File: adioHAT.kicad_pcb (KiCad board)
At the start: 2 copper layers, 65 x 56 mm, 29 parts, among them J1 Conn_01x01, J2 Conn_02x02_Odd_Even, J3 Conn_02x20_Odd_Even, J4 Conn_02x20_Odd_Even, U1 AD8603, U2 DAC7571, U3 AD5593R, U4 LM7321, U5 PCA9575D, U6 TXU0104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

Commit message: fixed i2c connections for ad5593
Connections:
- U3 pad 15: /SCL -> /SDA
- U3 pad 16: /SDA -> /SCL
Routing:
- net /SDA: track 55.2 -> 56.6 mm, vias 0 -> 2
- net /SCL: track 59.9 -> 59.2 mm
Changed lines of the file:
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@@
       (net 1 "GND") (pinfunction "GND") (pintype "power_in"))
     (pad "15" smd roundrect (at -0.25 -1.4375 270) (size 0.25 0.875) (layers "F.Cu" "F.Paste" "F.Mask") (roundrect_rratio 0.25)
-      (net 32 "/SCL") (pinfunction "SDA") (pintype "bidirectional"))
+      (net 31 "/SDA") (pinfunction "SDA") (pintype "bidirectional"))
     (pad "16" smd roundrect (at -0.75 -1.4375 270) (size 0.25 0.875) (layers "F.Cu" "F.Paste" "F.Mask") (roundrect_rratio 0.25)
-      (net 31 "/SDA") (pinfunction "SCL") (pintype "input"))
+      (net 32 "/SCL") (pinfunction "SCL") (pintype "input"))
     (model "${KICAD6_3DMODEL_DIR}/Package_CSP.3dshapes/LFCSP-16-1EP_3x3mm_P0.5mm_EP1.3x1.3mm.wrl"
       (offset (xyz 0 0 0))
@@
   (via (at 105.537 50.8) (size 0.6) (drill 0.3) (layers "F.Cu" "B.Cu") (free) (net 1))
   (via (at 125.7556 52.0956) (size 0.6) (drill 0.3) (layers "F.Cu" "B.Cu") (free) (net 1))
-  (via (at 140.8178 66.8784) (size 0.6) (drill 0.3) (layers "F.Cu" "B.Cu") (free) (net 1))
+  (via (at 141.351 67.31) (size 0.6) (drill 0.3) (layers "F.Cu" "B.Cu") (free) (net 1))
   (via (at 160.8584 60.0966) (size 0.6) (drill 0.3) (layers "F.Cu" "B.Cu") (free) (net 1))
   (via (at 160.274 81.661) (size 0.6) (drill 0.3) (layers "F.Cu" "B.Cu") (net 1))
@@
   (segment (start 128.69 48.77) (end 127.244 50.216) (width 0.3) (layer "B.Cu") (net 30))
   (segment (start 118.9126 69.6426) (end 114.797 65.527) (width 0.2) (layer "F.Cu") (net 31))
-  (segment (start 139.2965 67.9675) (end 139.7828 67.4812) (width 0.2) (layer "F.Cu") (net 31))
-  (segment (start 139.7828 65.2338) (end 138.811 64.262) (width 0.2) (layer "F.Cu") (net 31))
   (segment (start 135.745786 64.262) (end 117.983 64.262) (width 0.2) (layer "F.Cu") (net 31))
   (segment (start 135.755386 64.2716) (end 135.745786 64.262) (width 0.2) (layer "F.Cu") (net 31))
@@
   (segment (start 116.186 54.046) (end 116.186 62.465) (width 0.2) (layer "F.Cu") (net 31))
   (segment (start 116.186 62.465) (end 116.967 63.246) (width 0.2) (layer "F.Cu") (net 31))
+  (segment (start 138.852178 64.262) (end 139.121839 64.531661) (width 0.2) (layer "F.Cu") (net 31))
   (segment (start 117.983 64.262) (end 116.967 63.246) (width 0.2) (layer "F.Cu") (net 31))
-  (segment (start 139.7828 67.4812) (end 139.7828 65.2338) (width 0.2) (layer "F.Cu") (net 31))
+  (segment (start 139.616186 68.4675) (end 138.9653 68.4675) (width 0.2) (layer "F.Cu") (net 31))
   (segment (start 115.145896 65.527) (end 114.797 65.527) (width 0.2) (layer "F.Cu") (net 31))
   (segment (start 117.221 63.5) (end 117.172896 63.5) (width 0.2) (layer "F.Cu") (net 31))
   (segment (start 138.811 64.262) (end 136.593415 64.262) (width 0.2) (layer "F.Cu") (net 31))
   (segment (start 136.583814 64.2716) (end 135.755386 64.2716) (width 0.2) (layer "F.Cu") (net 31))
-  (segment (start 138.9653 67.9675) (end 139.2965 67.9675) (width 0.2) (layer "F.Cu") (net 31))
   (segment (start 110.91 48.77) (end 116.186 54.046) (width 0.2) (layer "F.Cu") (net 31))
   (segment (start 116.967 63.246) (end 117.221 63.5) (width 0.2) (layer "F.Cu") (net 31))
+  (segment (start 138.811 64.262) (end 138.852178 64.262) (width 0.2) (layer "F.Cu") (net 31))
   (segment (start 117.172896 63.5) (end 115.145896 65.527) (width 0.2) (layer "F.Cu") (net 31))
   (segment (start 118.9126 71.4912) (end 118.9126 69.6426) (width 0.2) (layer "F.Cu") (net 31))
-  (segment (start 136.41813 63.8716) (end 136.42773 63.862) (width 0.2) (layer "F.Cu") (net 32))
-  (segment (start 139.3 63.862) (end 140.1828 64.7448) (width 0.2) (layer "F.Cu") (net 32))
-  (segment (start 136.42773 63.862) (end 139.3 63.862) (width 0.2) (layer "F.Cu") (net 32))
+  (segment (start 140.567023 67.516663) (end 139.616186 68.4675) (width 0.2) (layer "F.Cu") (net 31))
+  (segment (start 140.567023 67.466795) (end 140.567023 67.516663) (width 0.2) (layer "F.Cu") (net 31))
+  (via (at 139.121839 64.531661) (size 0.6) (drill 0.3) (layers "F.Cu" "B.Cu") (net 31))
+  (via (at 140.567023 67.466795) (size 0.6) (drill 0.3) (layers "F.Cu" "B.Cu") (net 31))
+  (segment (start 140.567023 67.466795) (end 140.589 67.444818) (width 0.2) (layer "B.Cu") (net 31))
+  (segment (start 140.589 67.444818) (end 140.589 65.998822) (width 0.2) (layer "B.Cu") (net 31))
+  (segment (start 140.589 65.998822) (end 139.121839 64.531661) (width 0.2) (layer "B.Cu") (net 31))
+  (segment (start 117.602 62.992) (end 118.472 63.862) (width 0.2) (layer "F.Cu") (net 32))
+  (segment (start 135.921072 63.8716) (end 136.41813 63.8716) (width 0.2) (layer "F.Cu") (net 32))
+  (segment (start 135.911471 63.862) (end 135.921072 63.8716) (width 0.2) (layer "F.Cu") (net 32))
   (segment (start 115.786 64.173) (end 115.382 64.577) (width 0.2) (layer "F.Cu") (net 32))
   (segment (start 116.205 63.5) (end 115.786 63.919) (width 0.2) (layer "F.Cu") (net 32))
   (segment (start 116.459 68.072) (end 118.2626 69.8756) (width 0.2) (layer "F.Cu") (net 32))
   (segment (start 115.382 64.577) (end 114.797 64.577) (width 0.2) (layer "F.Cu") (net 32))
+  (segment (start 139.3 63.862) (end 139.827 64.389) (width 0.2) (layer "F.Cu") (net 32))
   (segment (start 113.45 50.6866) (end 116.586 53.8226) (width 0.2) (layer "F.Cu") (net 32))
-  (segment (start 135.911471 63.862) (end 135.921072 63.8716) (width 0.2) (layer "F.Cu") (net 32))
+  (segment (start 136.41813 63.8716) (end 136.42773 63.862) (width 0.2) (layer "F.Cu") (net 32))
   (segment (start 117.729 63.119) (end 117.602 62.992) (width 0.2) (layer "F.Cu") (net 32))
   (segment (start 113.45 48.77) (end 113.45 50.6866) (width 0.2) (layer "F.Cu") (net 32))
-  (segment (start 140.1828 67.700152) (end 139.415452 68.4675) (width 0.2) (layer "F.Cu") (net 32))
-  (segment (start 139.415452 68.4675) (end 138.9653 68.4675) (width 0.2) (layer "F.Cu") (net 32))
+  (segment (start 139.827 67.691) (end 139.5505 67.9675) (width 0.2) (layer "F.Cu") (net 32))
+  (segment (start 139.5505 67.9675) (end 138.9653 67.9675) (width 0.2) (layer "F.Cu") (net 32))
+  (segment (start 139.827 64.389) (end 139.827 67.691) (width 0.2) (layer "F.Cu") (net 32))
   (segment (start 115.786 63.919) (end 115.786 64.173) (width 0.2) (layer "F.Cu") (net 32))
-  (segment (start 140.1828 64.7448) (end 140.1828 67.700152) (width 0.2) (layer "F.Cu") (net 32))
   (segment (start 116.586 61.976) (end 117.602 62.992) (width 0.2) (layer "F.Cu") (net 32))
   (segment (start 115.316 68.072) (end 116.459 68.072) (width 0.2) (layer "F.Cu") (net 32))
-  (segment (start 117.602 62.992) (end 118.472 63.862) (width 0.2) (layer "F.Cu") (net 32))
+  (segment (start 118.472 63.862) (end 135.911471 63.862) (width 0.2) (layer "F.Cu") (net 32))
+  (segment (start 136.42773 63.862) (end 139.3 63.862) (width 0.2) (layer "F.Cu") (net 32))
   (segment (start 118.2626 69.8756) (end 118.2626 71.4912) (width 0.2) (layer "F.Cu") (net 32))
-  (segment (start 135.921072 63.8716) (end 136.41813 63.8716) (width 0.2) (layer "F.Cu") (net 32))
   (segment (start 116.586 53.8226) (end 116.586 61.976) (width 0.2) (layer "F.Cu") (net 32))
-  (segment (start 118.472 63.862) (end 135.911471 63.862) (width 0.2) (layer "F.Cu") (net 32))
   (via (at 116.205 63.5) (size 0.6) (drill 0.3) (layers "F.Cu" "B.Cu") (net 32))
   (via (at 117.729 63.119) (size 0.6) (drill 0.3) (layers "F.Cu" "B.Cu") (net 32))

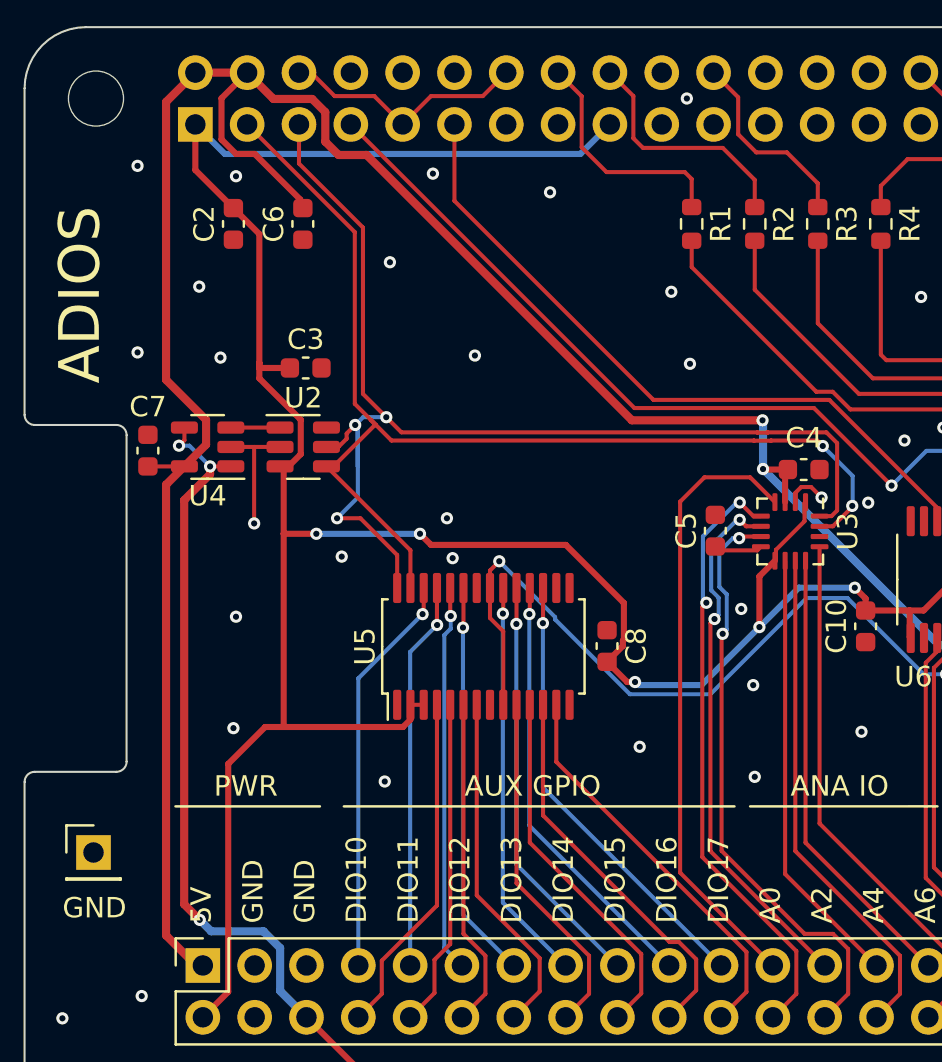
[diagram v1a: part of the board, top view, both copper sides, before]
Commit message: moved some elements inwards to increase border clearance
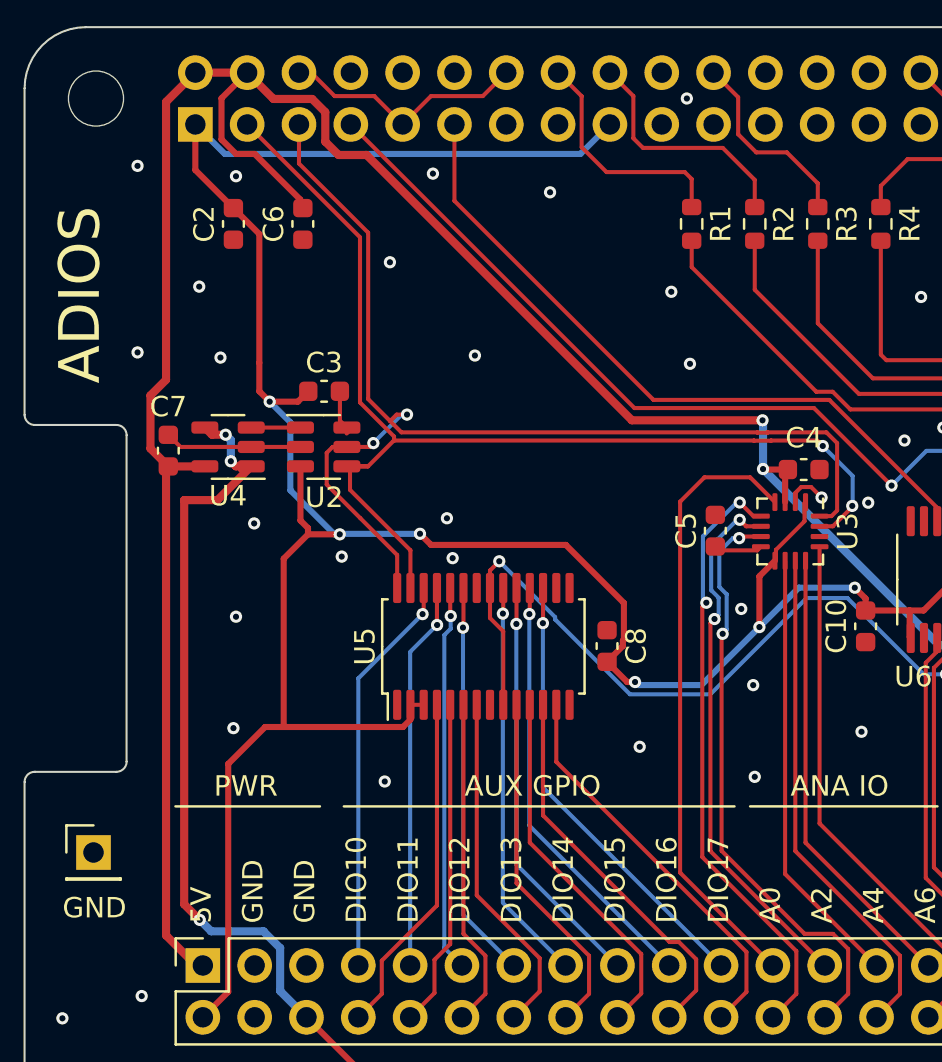
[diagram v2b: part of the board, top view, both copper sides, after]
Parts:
- moved C3 1.46 mm to (114.7, 61.8)
- moved C7 1.00 mm to (107.0, 64.8)
- moved U2 1.00 mm to (114.7, 64.6)
- moved U4 1.00 mm to (110.0, 64.6)
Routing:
- net +3V3: track 145.7 -> 150.5 mm, vias 5 -> 6
- net GND: track 35.4 -> 38.6 mm
- net /SCL: track 59.2 -> 56.8 mm, vias 3 -> 2
- net /VDUT: track 121.3 -> 122.8 mm
- net +5V: track 128.5 -> 127.6 mm

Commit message: added comment on VDIG
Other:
- board text added: "DIG IO and GPIO on VDIG (1.1V < VDIG < 3.7V)"
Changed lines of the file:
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@@
   (gr_line (start 162 44) (end 103 44)
     (stroke (width 0.1) (type solid)) (layer "Edge.Cuts"))
+  (gr_text "DIG IO and GPIO on VDIG (1.1V < VDIG < 3.7V)" (at 160.909 86.614) (layer "B.SilkS")
+    (effects (font (size 1.5 1.5) (thickness 0.2)) (justify left bottom mirror))
+  )
   (gr_text "LM7321" (at 130.81 64.4398) (layer "B.SilkS")
     (effects (font (size 1.5 1.5) (thickness 0.2)) (justify left bottom mirror))
